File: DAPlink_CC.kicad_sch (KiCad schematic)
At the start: 58 parts, among them U1 ZD25Q80BNIGR, U10 DIO32220LP10, U2 SL2.1S, U3 GD32F350G8U6, U4 LP5240HVF, U5 JW5393FSOTI, U6 HC32L110B6YA, U7 LP5240HVF, U8 DIO32220LP10, U9 DIO32220LP10, X1 002_Xtal-4

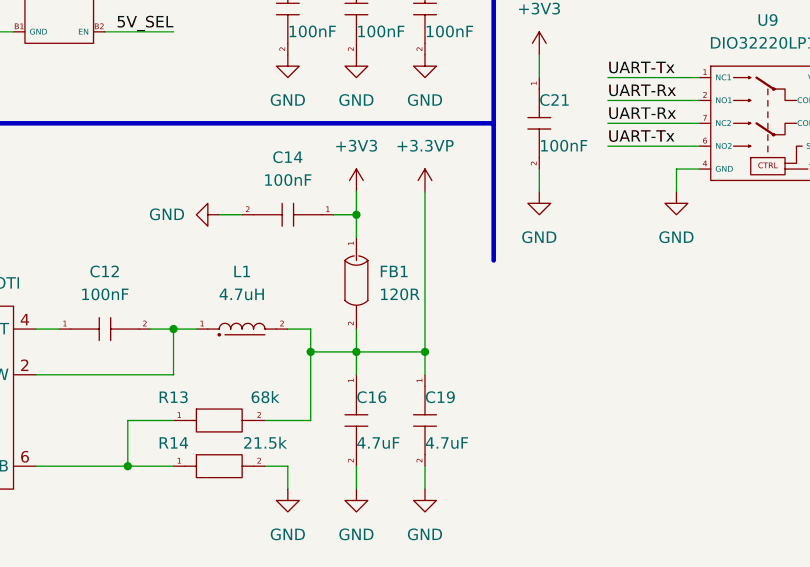
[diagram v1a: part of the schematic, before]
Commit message: Complete package assignments
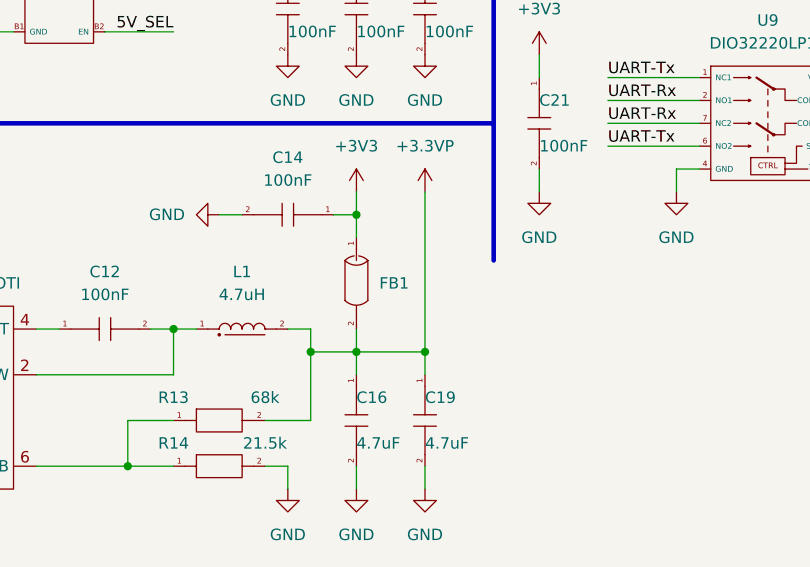
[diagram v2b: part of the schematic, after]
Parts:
- FB1: value 120R -> 120R_100MHz
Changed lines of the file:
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@@
   (symbol (lib_id "001_Basic_PassiveComponents:301_FerriteBead") (at 162.56 167.64 270) (unit 1)
     (in_bom yes) (on_board yes) (fields_autoplaced)
-    (property "Reference" "FB1" (id 0) (at 165.1 166.3699 90)
-      (effects (font (size 1.27 1.27)) (justify left))
-    )
-    (property "Value" "120R" (id 1) (at 165.1 168.9099 90)
-      (effects (font (size 1.27 1.27)) (justify left))
+    (property "Reference" "FB1" (id 0) (at 165.1 167.6399 90)
+      (effects (font (size 1.27 1.27)) (justify left))
+    )
+    (property "Value" "120R_100MHz" (id 1) (at 165.1 168.9099 90)
+      (effects (font (size 1.27 1.27)) (justify left) hide)
     )
     (property "Footprint" "001_GN_RCL_SMD:L0603(1608M)" (id 2) (at 167.64 167.64 0)
@@
     )
     (path "/de0f3acd-cb25-42b1-950d-bedb1d62762e"
-      (reference "FB1") (unit 1) (value "120R") (footprint "001_GN_RCL_SMD:L0603(1608M)")
+      (reference "FB1") (unit 1) (value "120R_100MHz") (footprint "001_GN_RCL_SMD:L0603(1608M)")
     )
     (path "/63e65823-a499-4fc9-83ba-7754dd13e5bf/4453fad0-3ecf-4d71-8ea8-f08497de193b"
-      (reference "J1") (unit 1) (value "USB_TypeC-24") (footprint "")
+      (reference "J1") (unit 1) (value "USB_TypeC-24") (footprint "206_CONN_USB:SCF-24_7925SST")
     )
     (path "/63e65823-a499-4fc9-83ba-7754dd13e5bf/37279274-71bb-46e2-8af9-b544d17bf0cc"

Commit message: Update layout
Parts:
- U6: footprint 104_SP_SMALL_SMD:CSP-16_1614 -> 003_GN_SMALL-SEMI_SMD:QFN-20_3030; symbol 107_IntegratedCircuit_MicroController:HC32L110B6YA -> MCU:HC32L110C6UA
- X1: value 002_Xtal-4 -> 12MHz; footprint 006_GN_XTAL_OSC_SMD:CXO-4_3225 -> 006_GN_XTAL_OSC_SMD:CXO-4_2520
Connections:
- net +3V3: now also U6.6 (Vin); no longer U6.C4 (Vin)
- net 3V3_SEL: now also U6.12 (P25); no longer U6.B1 (P25)
- net 5V_SEL: now also U6.13 (P26); no longer U6.A1 (P26)
- net AUX_SWCLK: now also U6.15 (P31); no longer U6.D4 (P31)
- net AUX_SWDIO: now also U6.14 (P27); no longer U6.D3 (P27)
- net DBG-RxN: now also U8.5 (COM2); no longer U8.3 (COM1)
- net DBG-RxP: now also U8.3 (COM1); no longer U8.5 (COM2)
- net DIR_SEL: now also U6.10 (P23); no longer U6.C2 (P23)
- net GND: now also U6.4 (GND); no longer U6.B4 (GND)
- net IDL-D: now also U6.9 (P14); no longer U6.D1 (P14)
- net Isns_N: now also U6.20 (P36); no longer U6.A3 (P36)
- net Isns_P: now also U6.19 (P35); no longer U6.A2 (P35)
- net JTAG_SEL: now also U6.11 (P24); no longer U6.C1 (P24)
- net UART-CC1: now also U6.2 (P01), U9.5 (COM2); no longer U6.B3 (P01), U9.3 (COM1)
- net UART-CC2: now also U6.3 (P02), U9.3 (COM1); no longer U6.A4 (P02), U9.5 (COM2)
- net UART-Rx: now also U8.1 (NC1), U9.1 (NC1), U9.6 (NO2); no longer U8.7 (NC2), U9.2 (NO1), U9.7 (NC2)
- net UART-Tx: now also U8.7 (NC2), U9.2 (NO1), U9.7 (NC2); no longer U8.1 (NC1), U9.1 (NC1), U9.6 (NO2)
- net ~{OE}: now also U6.8 (P15); no longer U6.D2 (P15)
- net at C23.1: now also U6.1 (~{RST}); no longer U6.B2 (~{RST})
- net at C22.1: now also U6.5 (Vcap); no longer U6.C3 (Vcap)

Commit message: Update layout
Nightly update
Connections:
- net DBG-RxN: now also U8.3 (COM1); no longer U8.5 (COM2)
- net DBG-RxP: now also U8.5 (COM2); no longer U8.3 (COM1)
- net SWCLK_TCK: now also U10.1 (NC1), U10.6 (NO2); no longer U10.2 (NO1), U10.7 (NC2)
- net SWDIO_TMS: now also U10.2 (NO1), U10.7 (NC2); no longer U10.1 (NC1), U10.6 (NO2)
- net SWO_TDO: now also U8.2 (NO1); no longer U8.6 (NO2)
- net TDI: now also U8.6 (NO2); no longer U8.2 (NO1)
- net UART-Rx: now also U8.7 (NC2); no longer U8.1 (NC1)
- net UART-Tx: now also U8.1 (NC1); no longer U8.7 (NC2)
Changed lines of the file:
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@@
     (effects (font (size 1.27 1.27)) (justify right bottom))
   )
-  (label "UART-Rx" (at 190.5 116.84 0)
+  (label "UART-Rx" (at 190.5 121.92 0)
     (effects (font (size 1.27 1.27)) (justify left bottom))
   )
@@
     (effects (font (size 1.27 1.27)) (justify right bottom))
   )
-  (label "SWCLK_TCK" (at 241.3 147.32 0)
+  (label "SWCLK_TCK" (at 241.3 152.4 0)
     (effects (font (size 1.27 1.27)) (justify left bottom))
   )
@@
     (effects (font (size 1.27 1.27)) (justify right bottom))
   )
-  (label "SWDIO_TMS" (at 241.3 144.78 0)
+  (label "SWDIO_TMS" (at 241.3 149.86 0)
     (effects (font (size 1.27 1.27)) (justify left bottom))
   )
@@
     (effects (font (size 1.27 1.27)) (justify right bottom))
   )
-  (label "TDI" (at 190.5 119.38 0)
+  (label "TDI" (at 190.5 124.46 0)
     (effects (font (size 1.27 1.27)) (justify left bottom))
   )
@@
     (effects (font (size 1.27 1.27)) (justify left bottom))
   )
-  (label "DBG-RxN" (at 226.06 121.92 180)
+  (label "DBG-RxN" (at 226.06 119.38 180)
     (effects (font (size 1.27 1.27)) (justify right bottom))
   )
@@
     (effects (font (size 1.27 1.27)) (justify left bottom))
   )
-  (label "SWDIO_TMS" (at 241.3 152.4 0)
+  (label "SWDIO_TMS" (at 241.3 147.32 0)
     (effects (font (size 1.27 1.27)) (justify left bottom))
   )
@@
     (effects (font (size 1.27 1.27)) (justify left bottom))
   )
-  (label "SWCLK_TCK" (at 241.3 149.86 0)
+  (label "SWCLK_TCK" (at 241.3 144.78 0)
     (effects (font (size 1.27 1.27)) (justify left bottom))
   )
@@
     (effects (font (size 1.27 1.27)) (justify left bottom))
   )
-  (label "DBG-RxP" (at 226.06 119.38 180)
+  (label "DBG-RxP" (at 226.06 121.92 180)
     (effects (font (size 1.27 1.27)) (justify right bottom))
   )
@@
     (effects (font (size 1.27 1.27)) (justify left bottom))
   )
-  (label "UART-Tx" (at 190.5 121.92 0)
+  (label "UART-Tx" (at 190.5 116.84 0)
     (effects (font (size 1.27 1.27)) (justify left bottom))
   )
@@
     (effects (font (size 1.27 1.27)) (justify left bottom))
   )
-  (label "SWO_TDO" (at 190.5 124.46 0)
-    (effects (font (size 1.27 1.27)) (justify left bottom))
-  )
+  (label "SWO_TDO" (at 190.5 119.38 0)
+    (effects (font (size 1.27 1.27)) (justify left bottom))
+  )

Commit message: Nightly update
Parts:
- C13, C15, C18: footprint 001_GN_RCL_SMD:C0201(0603M) -> 001_GN_RCL_SMD:C0402(1005M)
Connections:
- net VBUS is gone; now on net +5VP: C15.1
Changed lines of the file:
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@@
       (effects (font (size 1.27 1.27)) (justify left))
     )
-    (property "Footprint" "001_GN_RCL_SMD:C0201(0603M)" (id 2) (at 160.02 137.16 0)
+    (property "Footprint" "001_GN_RCL_SMD:C0402(1005M)" (id 2) (at 160.02 137.16 0)
       (effects (font (size 1.27 1.27)) hide)
     )
@@
       (effects (font (size 1.27 1.27)) (justify left))
     )
-    (property "Footprint" "001_GN_RCL_SMD:C0201(0603M)" (id 2) (at 175.26 137.16 0)
+    (property "Footprint" "001_GN_RCL_SMD:C0402(1005M)" (id 2) (at 175.26 137.16 0)
       (effects (font (size 1.27 1.27)) hide)
     )
@@
     (pin "2")
   )
-  (symbol (lib_id "PowerPort:VBUS") (at 162.56 132.08 0) (unit 1)
-    (in_bom yes) (on_board yes) (fields_autoplaced)
-    (property "Reference" "#PWR047" (id 0) (at 162.56 135.89 0)
-      (effects (font (size 1.27 1.27)) hide)
-    )
-    (property "Value" "VBUS" (id 1) (at 162.56 127 0))
-    (property "Footprint" "" (id 2) (at 162.56 132.08 0)
-      (effects (font (size 1.27 1.27)) hide)
-    )
-    (property "Datasheet" "" (id 3) (at 162.56 132.08 0)
-      (effects (font (size 1.27 1.27)) hide)
-    )
-    (pin "1")
-  )
   (symbol (lib_id "PowerPort:GND") (at 170.18 99.06 0) (mirror y) (unit 1)
     (in_bom yes) (on_board yes) (fields_autoplaced)
@@
     (pin "1")
   )
+  (symbol (lib_id "PowerPort:+5VP") (at 162.56 132.08 0) (unit 1)
+    (in_bom yes) (on_board yes) (fields_autoplaced)
+    (property "Reference" "#PWR0103" (id 0) (at 162.56 135.89 0)
+      (effects (font (size 1.27 1.27)) hide)
+    )
+    (property "Value" "+5VP" (id 1) (at 162.56 127 0))
+    (property "Footprint" "" (id 2) (at 162.56 132.08 0)
+      (effects (font (size 1.27 1.27)) hide)
+    )
+    (property "Datasheet" "" (id 3) (at 162.56 132.08 0)
+      (effects (font (size 1.27 1.27)) hide)
+    )
+    (pin "1")
+  )
   (symbol (lib_id "001_Basic_PassiveComponents:001_Resistor") (at 208.28 132.08 0) (unit 1)
     (in_bom yes) (on_board yes)
@@
       (effects (font (size 1.27 1.27)) (justify left))
     )
-    (property "Footprint" "001_GN_RCL_SMD:C0201(0603M)" (id 2) (at 167.64 137.16 0)
+    (property "Footprint" "001_GN_RCL_SMD:C0402(1005M)" (id 2) (at 167.64 137.16 0)
       (effects (font (size 1.27 1.27)) hide)
     )
@@
       (reference "#PWR046") (unit 1) (value "+3V3") (footprint "")
     )
-    (path "/63e35888-7e33-4d3f-8efd-874d30d0b602"
-      (reference "#PWR047") (unit 1) (value "VBUS") (footprint "")
-    )
     (path "/e4cfe593-5cbd-43a1-a612-dcd9876f76dd"
       (reference "#PWR048") (unit 1) (value "GND") (footprint "")
@@
       (reference "#PWR0102") (unit 1) (value "VDC") (footprint "")
     )
+    (path "/a02860f2-0655-4205-b2ee-27e2af2e346f"
+      (reference "#PWR0103") (unit 1) (value "+5VP") (footprint "")
+    )
     (path "/633d0c7e-019e-4122-b2c7-1df570f36270"
       (reference "C1") (unit 1) (value "10pF") (footprint "001_GN_RCL_SMD:C0201(0603M)")
@@
     )
     (path "/056ea6ae-7768-49a5-a364-493a67c302f2"
-      (reference "C13") (unit 1) (value "100nF") (footprint "001_GN_RCL_SMD:C0201(0603M)")
+      (reference "C13") (unit 1) (value "100nF") (footprint "001_GN_RCL_SMD:C0402(1005M)")
     )
     (path "/afc2c77d-8304-4c7a-860c-7d54a10a51a6"
@@
     )
     (path "/e5ef9a17-ff61-4026-9061-610ac378a72e"
-      (reference "C15") (unit 1) (value "100nF") (footprint "001_GN_RCL_SMD:C0201(0603M)")
+      (reference "C15") (unit 1) (value "100nF") (footprint "001_GN_RCL_SMD:C0402(1005M)")
     )
     (path "/e2c42708-2c2b-4361-9288-da7eda424ad5"
@@
     )
     (path "/1c188069-ee68-4fa9-b6f4-f0d293caf79a"
-      (reference "C18") (unit 1) (value "100nF") (footprint "001_GN_RCL_SMD:C0201(0603M)")
+      (reference "C18") (unit 1) (value "100nF") (footprint "001_GN_RCL_SMD:C0402(1005M)")
     )
     (path "/79427b9c-09b0-4e0a-80be-69439e933aef"
@@
     )
     (path "/63e65823-a499-4fc9-83ba-7754dd13e5bf/02f0b071-4e62-4847-9c83-33aebd872bd8"
-      (reference "R18") (unit 1) (value "100k") (footprint "001_GN_RCL_SMD:R0201(0603M)")
+      (reference "R18") (unit 1) (value "100k") (footprint "001_GN_RCL_SMD:R0402(1005M)")
     )
     (path "/63e65823-a499-4fc9-83ba-7754dd13e5bf/2cac6749-8ea4-44ea-8652-1f30a59eec44"
@@
     )
     (path "/63e65823-a499-4fc9-83ba-7754dd13e5bf/20d2b459-8de7-491e-b910-92240af2c5d9"
-      (reference "R20") (unit 1) (value "100k") (footprint "001_GN_RCL_SMD:R0201(0603M)")
+      (reference "R20") (unit 1) (value "100k") (footprint "001_GN_RCL_SMD:R0402(1005M)")
     )
     (path "/4d68af14-1ca3-403c-93af-01761416c10e"

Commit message: Daily update
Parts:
- NT3, NT4: now left out of the parts list
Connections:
- net GND: now also U6.EP
- no-connect marks 8 -> 12
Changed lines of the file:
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@@
   (junction (at 170.18 96.52) (diameter 0) (color 0 0 0 0)
   )
+  (junction (at 175.26 93.98) (diameter 0) (color 0 0 0 0)
+  )
   (junction (at 170.18 160.02) (diameter 0) (color 0 0 0 0)
   )
@@
   )
   (no_connect (at 220.98 45.72))
+  (no_connect (at 190.5 101.6))
+  (no_connect (at 193.04 101.6))
   (no_connect (at 144.78 25.4))
+  (no_connect (at 195.58 101.6))
   (no_connect (at 66.04 116.84))
   (no_connect (at 144.78 30.48))
   (no_connect (at 66.04 129.54))
   (no_connect (at 66.04 127))
+  (no_connect (at 198.12 101.6))
   (no_connect (at 66.04 114.3))
   (no_connect (at 220.98 40.64))
@@
     (stroke (width 0) (type default) (color 0 0 0 0))
   )
+  (wire (pts (xy 175.26 91.44) (xy 175.26 93.98))
+    (stroke (width 0) (type default) (color 0 0 0 0))
+  )
   (wire (pts (xy 162.56 175.26) (xy 162.56 177.8))
     (stroke (width 0) (type default) (color 0 0 0 0))
@@
     (stroke (width 0) (type default) (color 0 0 0 0))
   )
+  (wire (pts (xy 177.8 91.44) (xy 175.26 91.44))
+    (stroke (width 0) (type default) (color 0 0 0 0))
+  )
   (wire (pts (xy 144.78 93.98) (xy 160.02 93.98))
     (stroke (width 0) (type default) (color 0 0 0 0))
@@
   )
   (symbol (lib_id "300_Link_NetCNVT:NetCNVT-2") (at 241.3 66.04 0) (unit 1)
-    (in_bom yes) (on_board yes) (fields_autoplaced)
+    (in_bom no) (on_board yes) (fields_autoplaced)
     (property "Reference" "NT4" (id 0) (at 241.3 63.5 0))
     (property "Value" "NetCNVT-2" (id 1) (at 241.3 63.5 0)
@@
   )
   (symbol (lib_id "300_Link_NetCNVT:NetCNVT-2") (at 241.3 60.96 0) (unit 1)
-    (in_bom yes) (on_board yes) (fields_autoplaced)
+    (in_bom no) (on_board yes) (fields_autoplaced)
     (property "Reference" "NT3" (id 0) (at 241.3 58.42 0))
     (property "Value" "NetCNVT-2" (id 1) (at 241.3 58.42 0)
@@
     (pin "2")
   )
-  (symbol (lib_id "MCU:HC32L110C6UA") (at 193.04 88.9 0) (unit 1)
+  (symbol (lib_name "HC32L110C6UA_1") (lib_id "MCU:HC32L110C6UA") (at 193.04 88.9 0) (unit 1)
     (in_bom yes) (on_board yes) (fields_autoplaced)
     (property "Reference" "U6" (id 0) (at 193.04 76.2 0))
@@
     )
     (pin "1")
+    (pin "16")
+    (pin "17")
+    (pin "18")
     (pin "4")
     (pin "5")
     (pin "6")
+    (pin "7")
+    (pin "EP")
     (pin "10")
     (pin "11")
